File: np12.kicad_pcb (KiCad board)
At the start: 2 copper layers, 78 x 81 mm, 43 parts, among them K1 KEYSW, K10 KEYSW, K11 KEYSW, K12 KEYSW, K2 KEYSW, K3 KEYSW, K4 KEYSW, K5 KEYSW, K6 KEYSW, K7 KEYSW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

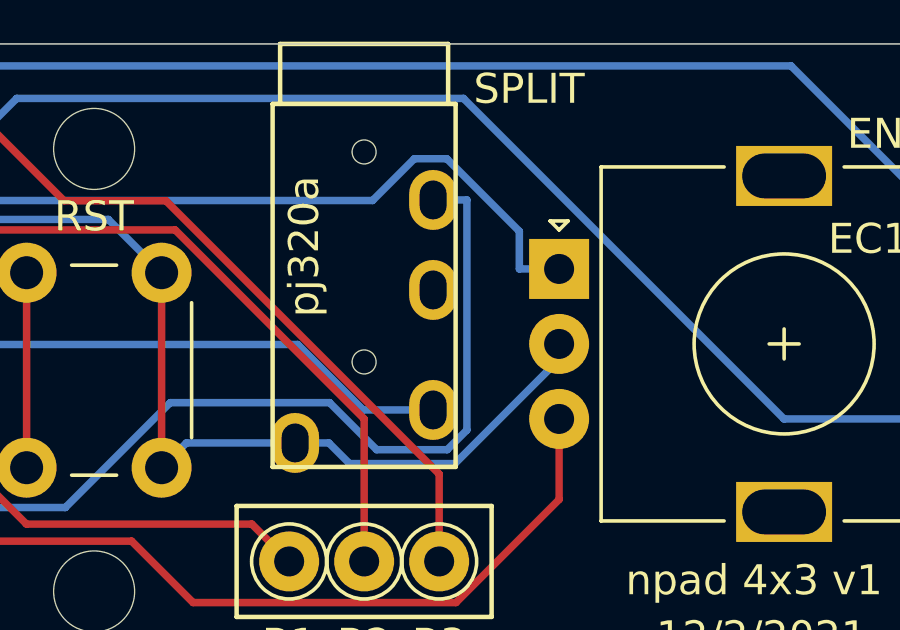
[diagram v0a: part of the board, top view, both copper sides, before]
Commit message: change split data trrs ring to ring 1
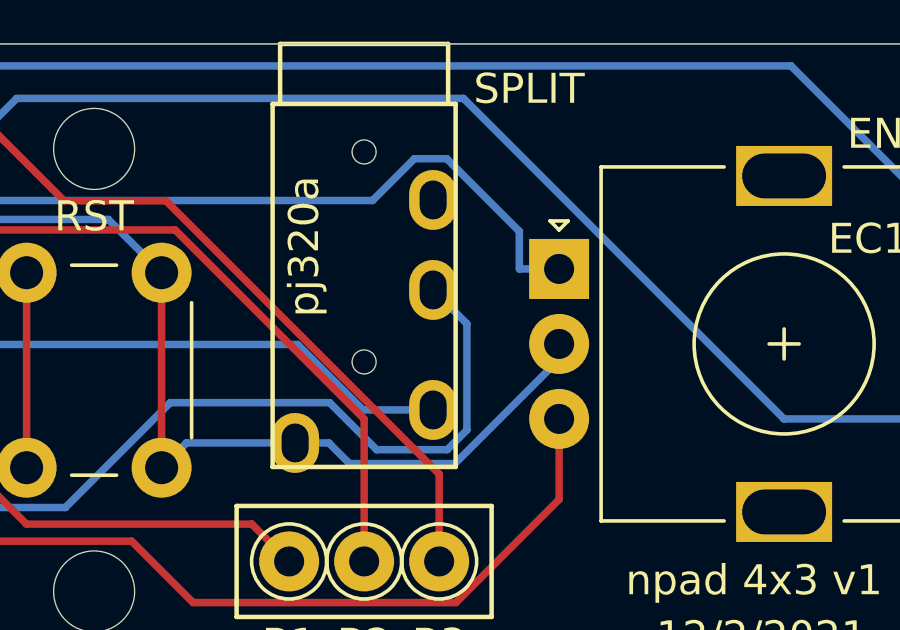
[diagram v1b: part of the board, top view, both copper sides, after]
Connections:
- net /row3 renamed Net-(U1-Pad12)
- net /row4 renamed Net-(U1-Pad13)
- U2 pad 3: Net-(U2-Pad3) -> /data
- U2 pad 4: /data -> Net-(U2-Pad4)
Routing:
- net /data: track 55.7 -> 52.0 mm
